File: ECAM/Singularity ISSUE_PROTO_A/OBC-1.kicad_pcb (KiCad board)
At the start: 6 copper layers, 42.8 x 42.8 mm, 109 parts, among them J1 ERM8-020-X, J2 ERF6-020-X, J3 Conn_01x02_Female, Q1 MGSF1N02L, Q2 MGSF1N02L, U1 TPS62850x-Q1, U10 FM33256B, U11 TMS5701227CZWTQQ1, U2 TPS62850x-Q1, U3 LTC4353, U4 SN65HVD230M-EP, U5 SN65HVD230M-EP, U6 SN65HVD230M-EP, U8 S70FL01GS, X1 ASTMTXK-32.768KHZ

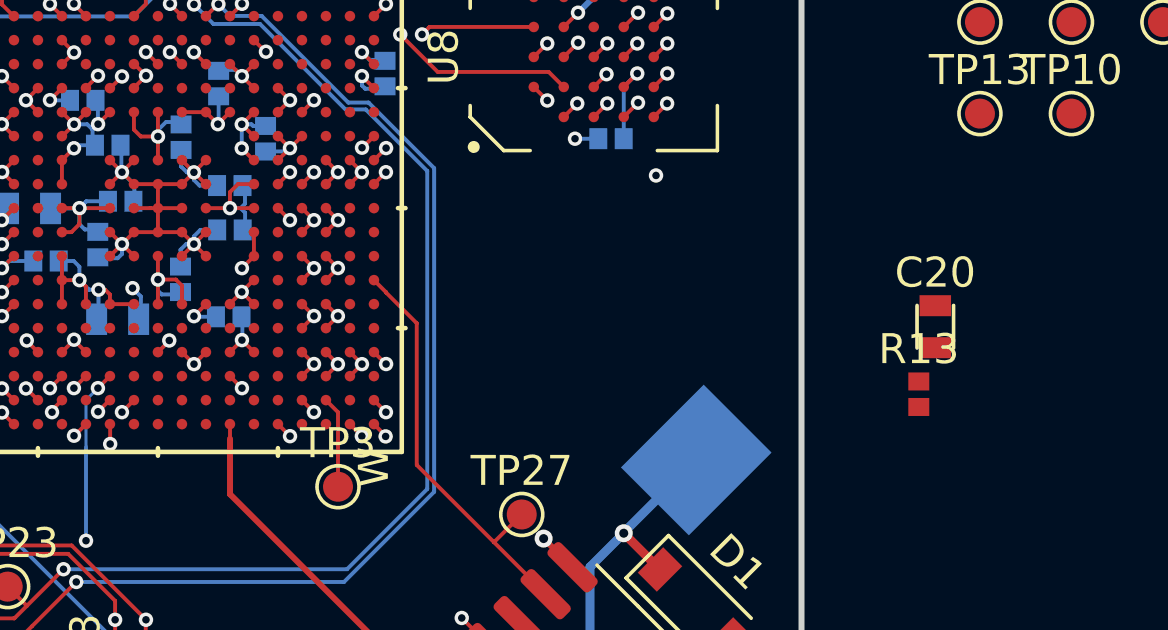
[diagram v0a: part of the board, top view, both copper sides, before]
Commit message: added FRAM to PCB layout
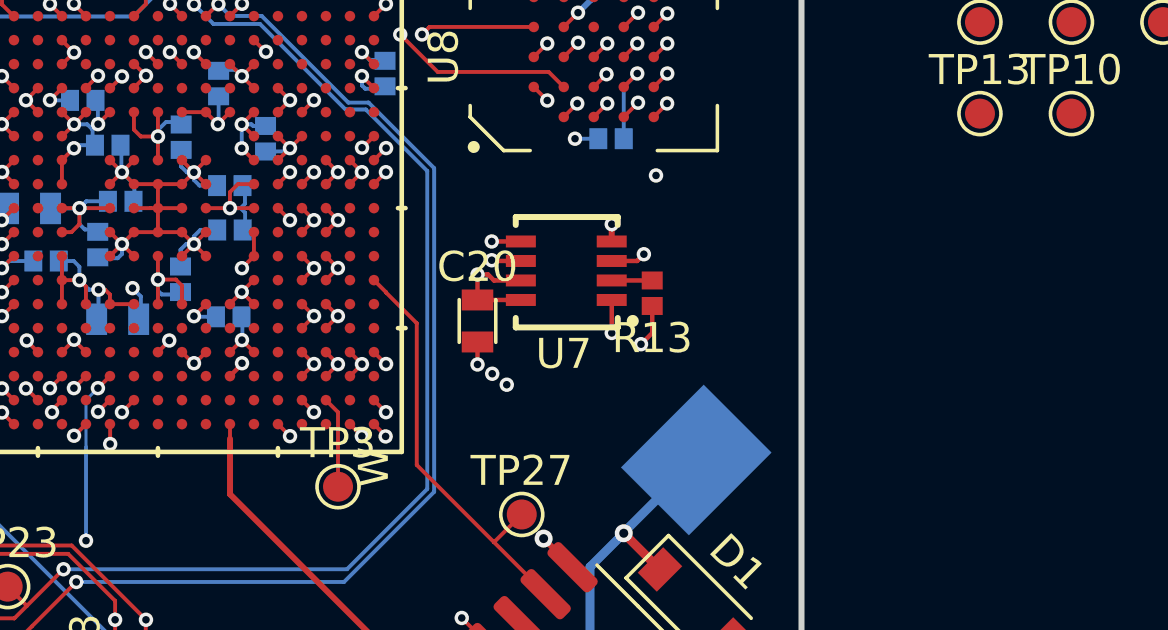
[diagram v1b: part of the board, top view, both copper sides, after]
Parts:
- added U7: CY15B108QI, TFT_GQFN:CY15B108QI, F.Cu at (125.4, 92.4)
- moved C20 15.3 mm to (120.9, 93.1)
- moved R13 9.50 mm to (126.7, 92.2), turned to 180 degrees
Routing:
- net /FRAM_1/FRAM_1_CLK: track 0.56 -> 26.7 mm, vias 1 -> 3
- net /FRAM_1/FRAM_1_COPI: track 0.56 -> 25.6 mm, vias 1 -> 3
- net /FRAM_1/FRAM_1_CIPO: track 0.56 -> 24.6 mm, vias 1 -> 2
- net /FRAM_1/FRAM_1_nCS: track 0.57 -> 14.4 mm, vias 1 -> 2
- net OBC_3V3: track 97.9 -> 102.9 mm, vias 31 -> 33
- net Net-(R13-Pad2): track 0.00 -> 1.35 mm
- net GND: track 195.9 -> 197.2 mm, vias 172 -> 174

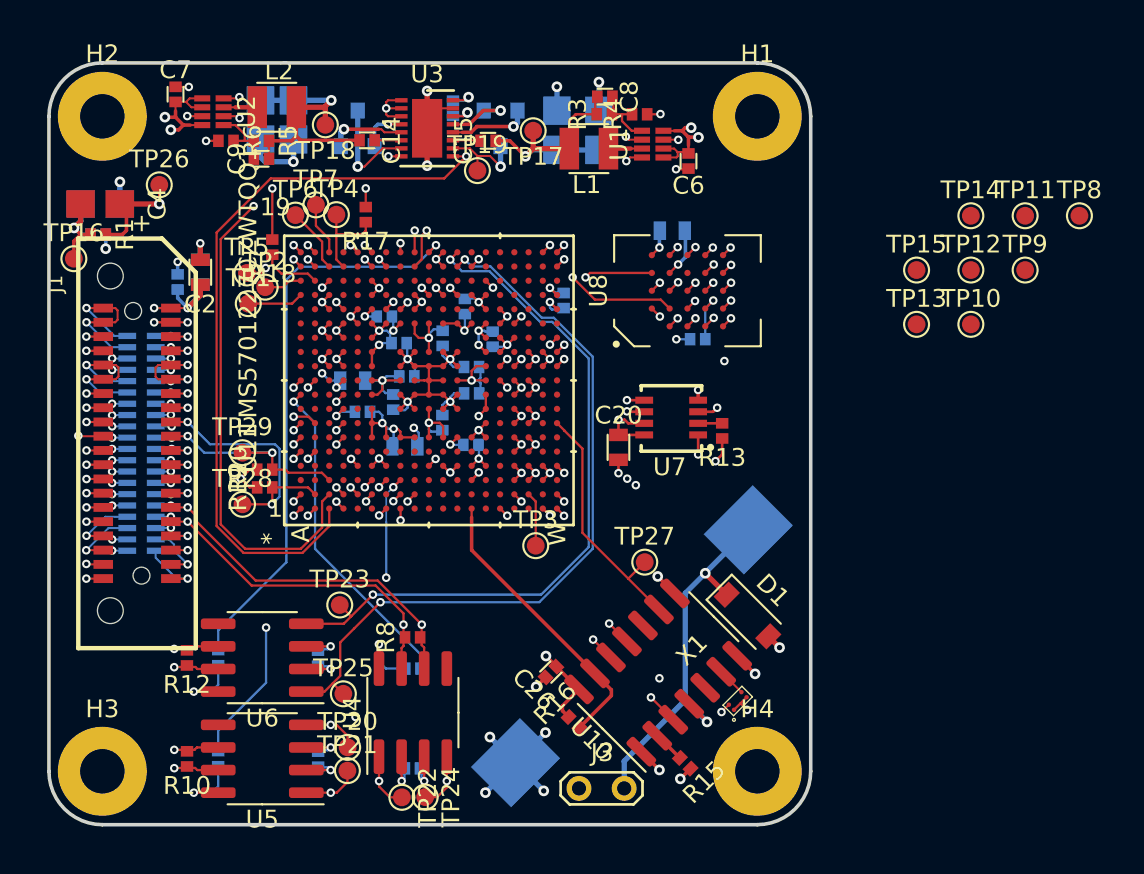
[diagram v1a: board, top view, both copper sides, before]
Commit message: added ground test points, adjusted trace width on RTC XTAL
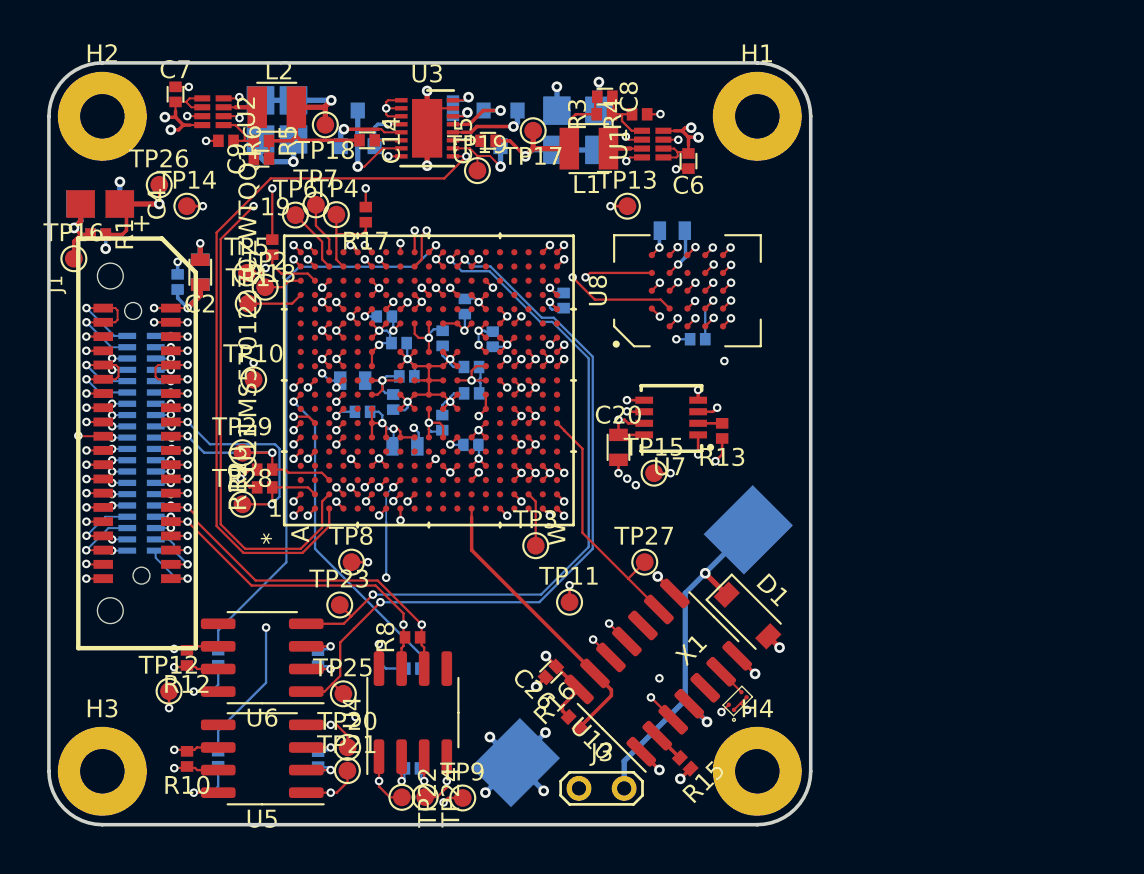
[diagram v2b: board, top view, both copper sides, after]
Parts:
- moved TP12 50.9 mm to (95.7, 106.8)
- moved TP8 45.3 mm to (105.9, 99.5)
- moved TP14 44.1 mm to (96.7, 79.5)
- moved TP9 43.3 mm to (112.2, 112.8)
- moved TP10 40.4 mm to (100.4, 89.3)
- moved TP11 33.6 mm to (118.2, 101.8)
- moved TP15 18.6 mm to (122.9, 94.5)
- moved TP13 17.6 mm to (121.4, 79.5)
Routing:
- net GND: track 197.2 -> 204.9 mm, vias 174 -> 182
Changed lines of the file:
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@@
     (thickness 1.6)
     (drawings 8)
-    (tracks 1740)
+    (tracks 1757)
     (zones 0)
     (modules 110)
@@
   )
   (module TFT_TestPoints:TP_RDPad_D1.0mm (layer F.Cu)
-    (at 137.6483 83.1382)
+    (at 122.9 94.55)
     (descr "SMD pad as test Point, diameter 1.0mm")
     (tags "test point SMD pad")
@@
   )
   (module TFT_TestPoints:TP_RDPad_D1.0mm (layer F.Cu)
-    (at 140.6983 80.0882)
+    (at 96.65 79.55)
     (descr "SMD pad as test Point, diameter 1.0mm")
     (tags "test point SMD pad")
@@
   )
   (module TFT_TestPoints:TP_RDPad_D1.0mm (layer F.Cu)
-    (at 137.6483 86.1882)
+    (at 121.4 79.55)
     (descr "SMD pad as test Point, diameter 1.0mm")
     (tags "test point SMD pad")
@@
   )
   (module TFT_TestPoints:TP_RDPad_D1.0mm (layer F.Cu)
-    (at 140.6983 83.1382)
+    (at 95.65 106.8)
     (descr "SMD pad as test Point, diameter 1.0mm")
     (tags "test point SMD pad")
@@
   )
   (module TFT_TestPoints:TP_RDPad_D1.0mm (layer F.Cu)
-    (at 143.7483 80.0882)
+    (at 118.15 101.8)
     (descr "SMD pad as test Point, diameter 1.0mm")
     (tags "test point SMD pad")
@@
   )
   (module TFT_TestPoints:TP_RDPad_D1.0mm (layer F.Cu)
-    (at 140.6983 86.1882)
+    (at 100.4 89.3)
     (descr "SMD pad as test Point, diameter 1.0mm")
     (tags "test point SMD pad")
@@
   )
   (module TFT_TestPoints:TP_RDPad_D1.0mm (layer F.Cu)
-    (at 143.7483 83.1382)
+    (at 112.15 112.8)
     (descr "SMD pad as test Point, diameter 1.0mm")
     (tags "test point SMD pad")
@@
   )
   (module TFT_TestPoints:TP_RDPad_D1.0mm (layer F.Cu)
-    (at 146.7983 80.0882)
+    (at 105.9 99.55)
     (descr "SMD pad as test Point, diameter 1.0mm")
     (tags "test point SMD pad")
@@
   (segment (start 124.059693 101.309693) (end 123.103812 100.353812) (width 0.2) (layer F.Cu) (net 2))
   (via (at 128.125 107.85) (size 0.48) (drill 0.25) (layers F.Cu B.Cu) (net 2))
-  (segment (start 127.769957 107.494957) (end 128.125 107.85) (width 0.13) (layer F.Cu) (net 2))
-  (segment (start 127.769957 107.469957) (end 127.769957 107.494957) (width 0.13) (layer F.Cu) (net 2))
-  (segment (start 128.09851 107.141403) (end 127.769957 107.469957) (width 0.13) (layer F.Cu) (net 2))
-  (segment (start 127.769957 107.469957) (end 127.391403 107.84851) (width 0.13) (layer F.Cu) (net 2))
+  (segment (start 127.769957 107.494957) (end 128.125 107.85) (width 0.115) (layer F.Cu) (net 2))
+  (segment (start 127.769957 107.469957) (end 127.769957 107.494957) (width 0.115) (layer F.Cu) (net 2))
+  (segment (start 128.09851 107.141403) (end 127.769957 107.469957) (width 0.115) (layer F.Cu) (net 2))
+  (segment (start 127.769957 107.469957) (end 127.391403 107.84851) (width 0.115) (layer F.Cu) (net 2))
   (via (at 109.85 84.925) (size 0.48) (drill 0.25) (layers F.Cu B.Cu) (net 2))
   (segment (start 109.44792 85.32708) (end 109.85 84.925) (width 0.13) (layer F.Cu) (net 2))
@@
   (segment (start 115.847919 94.14128) (end 116.2472 94.54056) (width 0.13) (layer F.Cu) (net 2))
   (segment (start 120.9 93.8) (end 120.9 94.55) (width 0.15) (layer F.Cu) (net 2))
+  (via (at 106.825 99.55) (size 0.48) (drill 0.25) (layers F.Cu B.Cu) (net 2))
+  (segment (start 105.9 99.55) (end 106.825 99.55) (width 0.15) (layer F.Cu) (net 2))
+  (via (at 100.4 88.35) (size 0.48) (drill 0.25) (layers F.Cu B.Cu) (net 2))
+  (segment (start 100.4 89.3) (end 100.4 88.35) (width 0.15) (layer F.Cu) (net 2))
+  (via (at 97.55 79.55) (size 0.48) (drill 0.25) (layers F.Cu B.Cu) (net 2))
+  (segment (start 96.65 79.55) (end 97.55 79.55) (width 0.15) (layer F.Cu) (net 2))
+  (via (at 120.45 79.55) (size 0.48) (drill 0.25) (layers F.Cu B.Cu) (net 2))
+  (segment (start 121.4 79.55) (end 120.45 79.55) (width 0.15) (layer F.Cu) (net 2))
+  (via (at 123.825 94.55) (size 0.48) (drill 0.25) (layers F.Cu B.Cu) (net 2))
+  (segment (start 122.9 94.55) (end 123.825 94.55) (width 0.15) (layer F.Cu) (net 2))
+  (via (at 118.15 100.85) (size 0.48) (drill 0.25) (layers F.Cu B.Cu) (net 2))
+  (segment (start 118.15 101.8) (end 118.15 100.85) (width 0.15) (layer F.Cu) (net 2))
+  (via (at 111.075 113.05) (size 0.48) (drill 0.25) (layers F.Cu B.Cu) (net 2))
+  (segment (start 111.325 112.8) (end 111.075 113.05) (width 0.15) (layer F.Cu) (net 2))
+  (segment (start 112.15 112.8) (end 111.325 112.8) (width 0.15) (layer F.Cu) (net 2))
+  (via (at 95.65 107.75) (size 0.48) (drill 0.25) (layers F.Cu B.Cu) (net 2))
+  (segment (start 95.65 106.8) (end 95.65 107.75) (width 0.15) (layer F.Cu) (net 2))
   (segment (start 90.297 79.4367) (end 90.3079 79.4258) (width 0.2) (layer B.Cu) (net 3))
   (segment (start 90.3061 79.4258) (end 90.297 79.4349) (width 0.2) (layer F.Cu) (net 3))

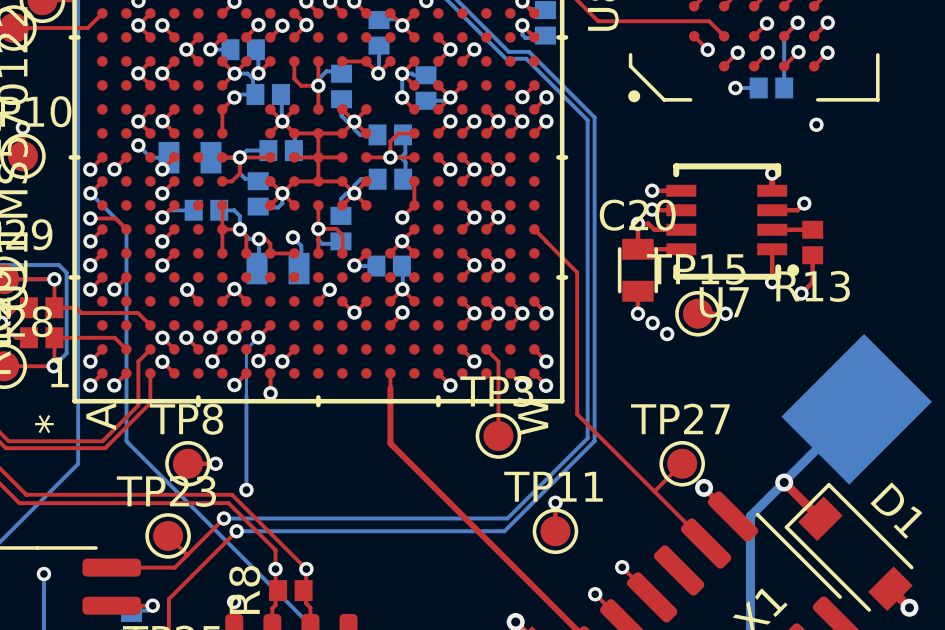
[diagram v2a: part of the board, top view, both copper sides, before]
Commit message: updated FRAM_CLK routing
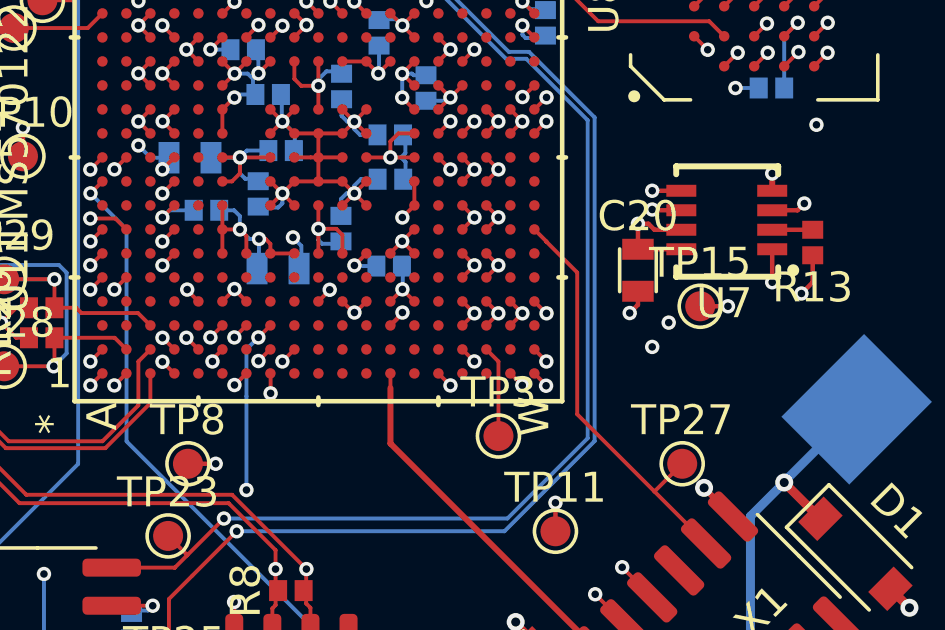
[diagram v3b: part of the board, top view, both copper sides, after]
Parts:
- moved TP15 0.26 mm to (123.0, 94.3)
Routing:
- net /FRAM_1/FRAM_1_CLK: track 26.7 -> 22.3 mm
